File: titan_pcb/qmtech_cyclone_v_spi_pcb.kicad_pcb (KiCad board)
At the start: 2 copper layers, 101.6 x 88.9 mm, 13 parts, among them J1 FPGA U8, J15 teensy3.2_left_header_double, J16 pico_right_header_double, J2 FPGA U7, J3 DUMMY_JTAG, J4 esp_right_header_double, J5 pico_left_header_double, J7 esp_left_header_double, J8 teensy3.2_right_header_double, U1 ESP32-DevKitC, U2 Teensy3.2, U3 Pico

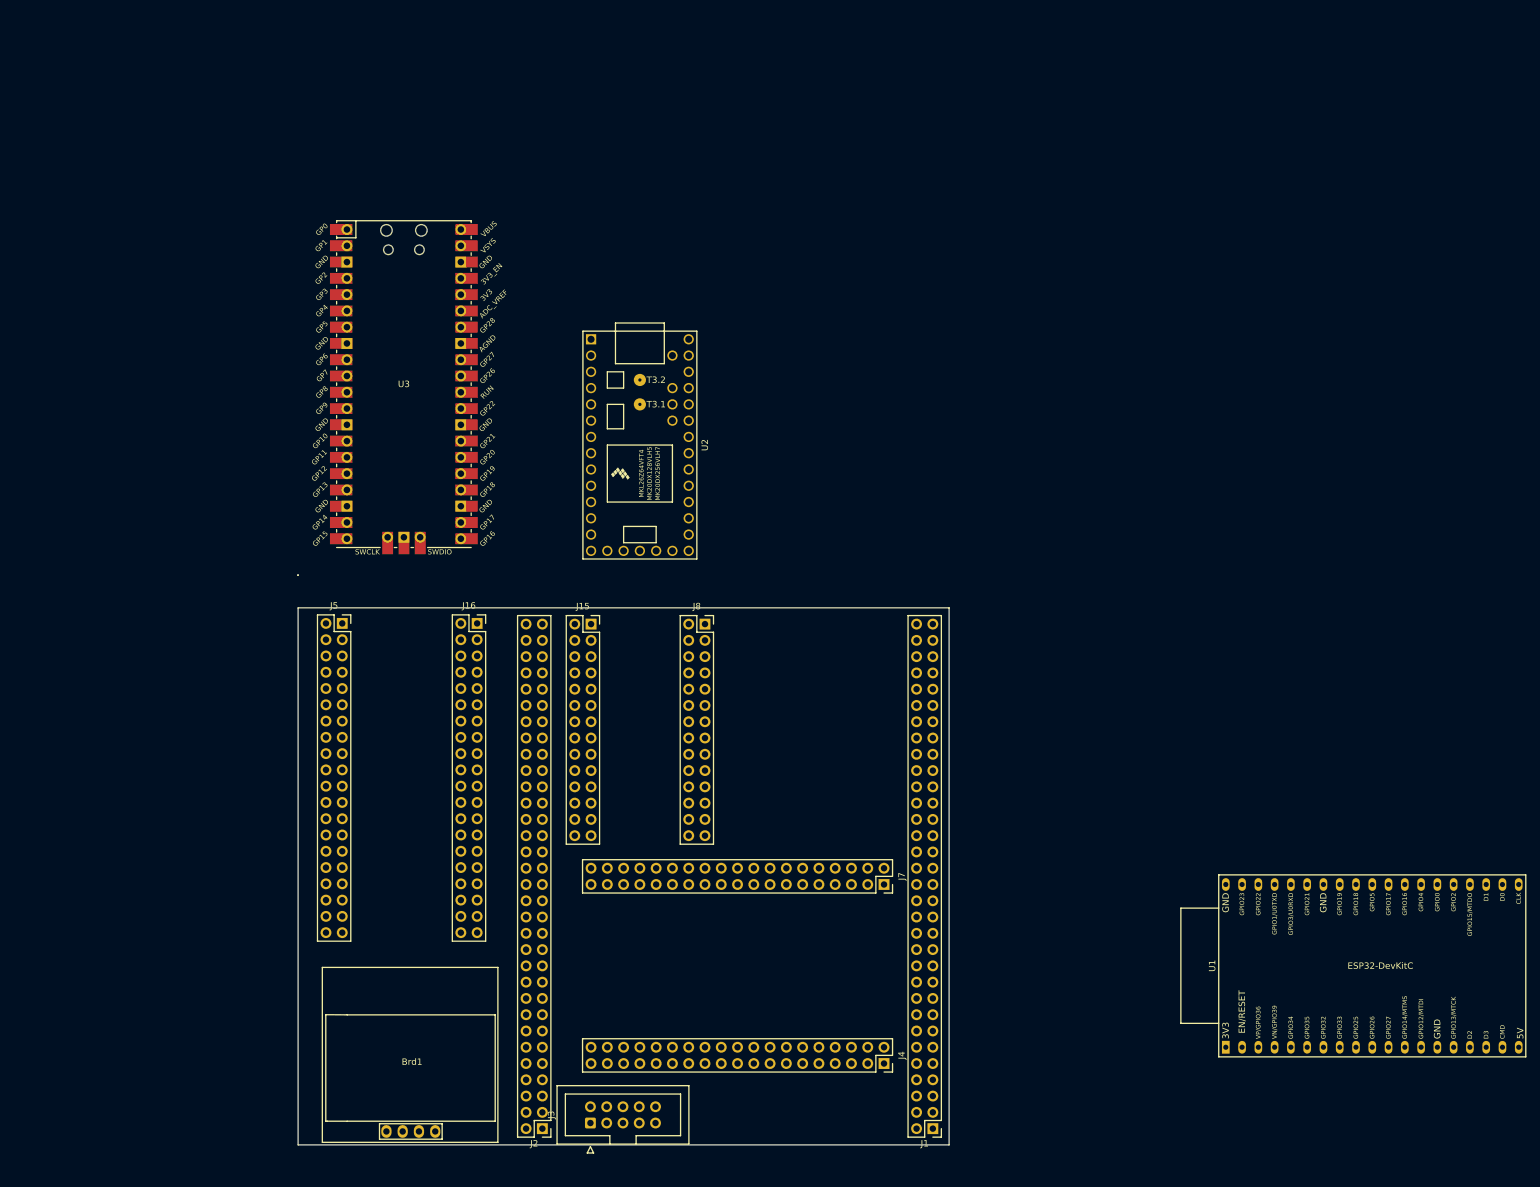
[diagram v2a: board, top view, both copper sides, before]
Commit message: finalised pcb - pinouts checked, silkscreen  and ground plane added
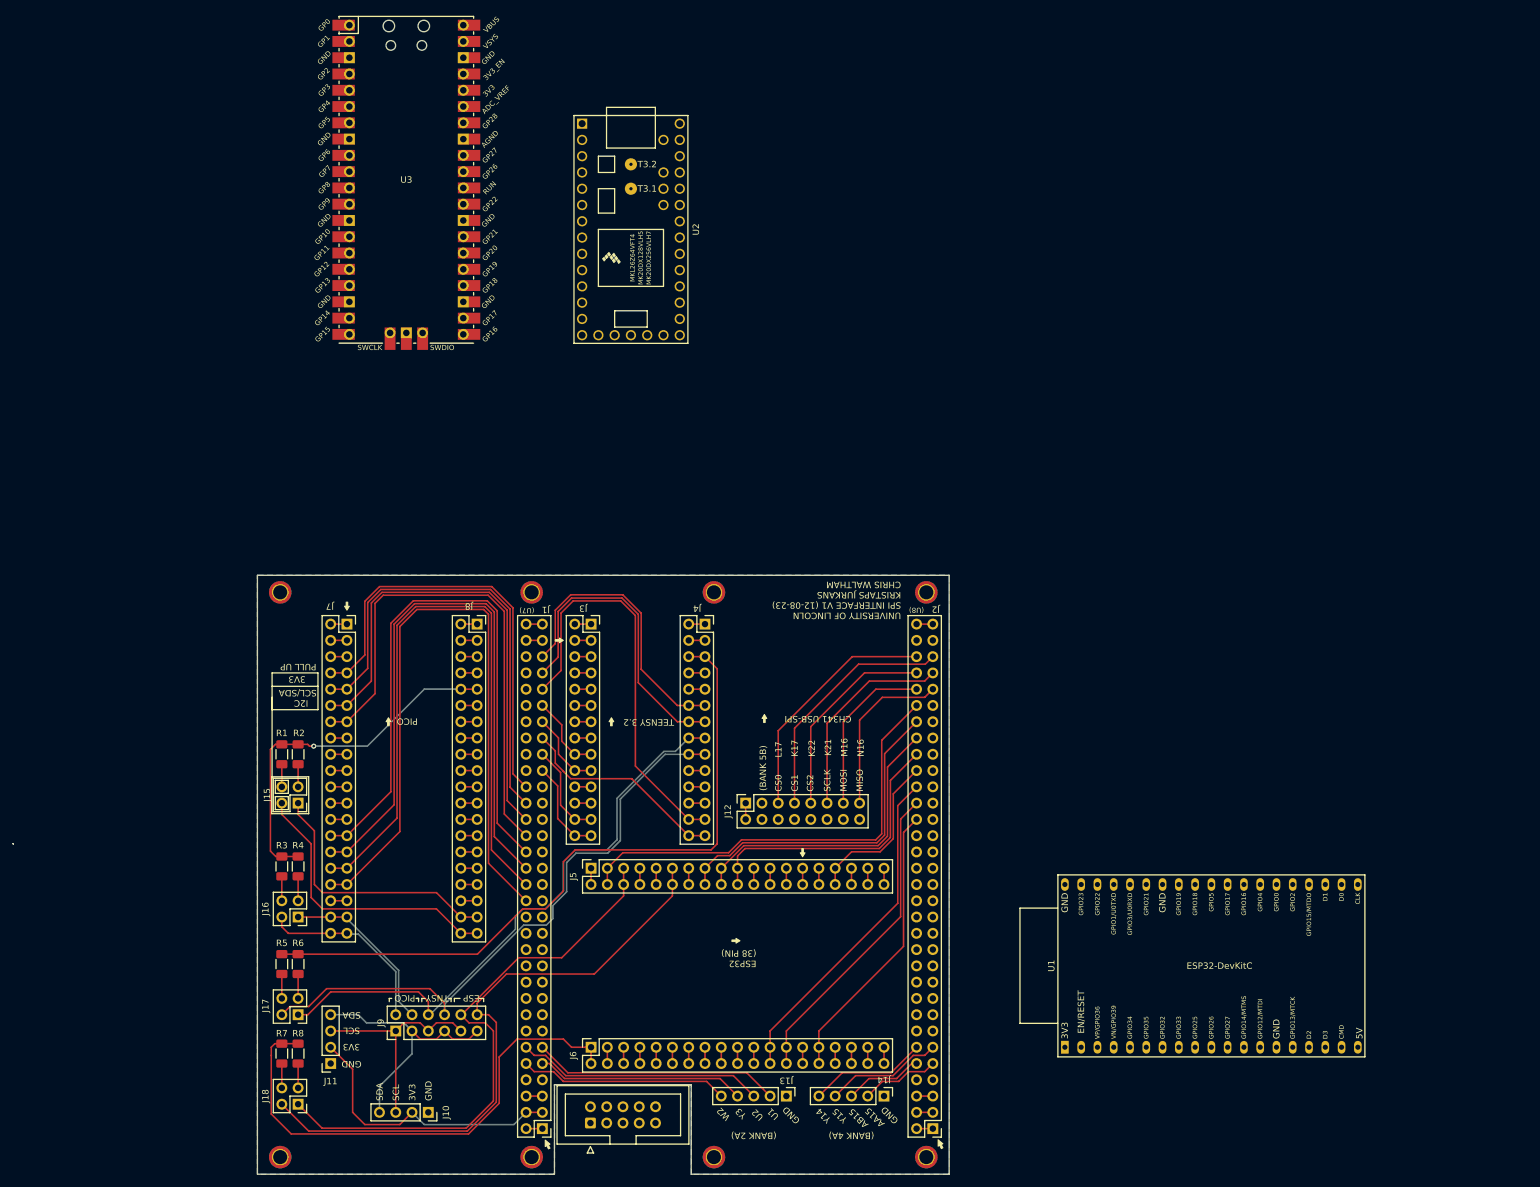
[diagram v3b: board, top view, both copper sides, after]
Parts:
- removed Brd1: OLED, SSD1306:128x64OLED
- added H1: MountingHole, MountingHole:MountingHole_2.2mm_M2_ISO7380_Pad_TopBottom, F.Cu at (48.0, 33.1)
- added H2: MountingHole, MountingHole:MountingHole_2.2mm_M2_ISO7380_Pad_TopBottom, F.Cu at (48.0, 121.3)
- added H3: MountingHole, MountingHole:MountingHole_2.2mm_M2_ISO7380_Pad_TopBottom, F.Cu at (87.2, 33.1)
- added H4: MountingHole, MountingHole:MountingHole_2.2mm_M2_ISO7380_Pad_TopBottom, F.Cu at (87.2, 121.3)
- added H5: MountingHole, MountingHole:MountingHole_2.2mm_M2_ISO7380_Pad_TopBottom, F.Cu at (148.8, 33.1)
- added H6: MountingHole, MountingHole:MountingHole_2.2mm_M2_ISO7380_Pad_TopBottom, F.Cu at (148.8, 121.3)
- added H7: MountingHole, MountingHole:MountingHole_2.2mm_M2_ISO7380_Pad_TopBottom, F.Cu at (115.7, 33.1)
- added H8: MountingHole, MountingHole:MountingHole_2.2mm_M2_ISO7380_Pad_TopBottom, F.Cu at (115.7, 121.3)
- added J10: OLED_CONN_0, Connector_PinSocket_2.54mm:PinSocket_1x04_P2.54mm_Vertical, F.Cu at (71.1, 114.3)
- added J11: OLED_CONN_1, Connector_PinSocket_2.54mm:PinSocket_1x04_P2.54mm_Vertical, F.Cu at (55.9, 106.7)
- added J12: CH341_PRG_CONN, Connector_PinSocket_2.54mm:PinSocket_2x08_P2.54mm_Vertical, F.Cu at (120.7, 66.0)
- added J13: SPI_HEADER_0, Connector_PinHeader_2.54mm:PinHeader_1x05_P2.54mm_Vertical, F.Cu at (127.0, 111.8)
- added J14: SPI_HEADER_1, Connector_PinHeader_2.54mm:PinHeader_1x05_P2.54mm_Vertical, F.Cu at (142.2, 111.8)
- added J15: PICO_I2C0_PULLUPS, Connector_PinHeader_2.54mm:PinHeader_2x02_P2.54mm_Vertical, F.Cu at (50.8, 66.0)
- added J16: PICO_I2C1_PULLUPS, Connector_PinHeader_2.54mm:PinHeader_2x02_P2.54mm_Vertical, F.Cu at (50.8, 83.8)
- added J17: TEENSY_I2C_PULLUPS, Connector_PinHeader_2.54mm:PinHeader_2x02_P2.54mm_Vertical, F.Cu at (50.8, 99.1)
- added J18: ESP32_I2C_PULLUPS, Connector_PinHeader_2.54mm:PinHeader_2x02_P2.54mm_Vertical, F.Cu at (50.8, 113.0)
- added J9: OLED_JMP, Connector_PinHeader_2.54mm:PinHeader_2x06_P2.54mm_Vertical, F.Cu at (66.0, 101.6)
- added R1: 2K, Resistor_SMD:R_1206_3216Metric_Pad1.30x1.75mm_HandSolder, F.Cu at (48.3, 58.4)
- added R2: 2K, Resistor_SMD:R_1206_3216Metric_Pad1.30x1.75mm_HandSolder, F.Cu at (50.8, 58.4)
- added R3: 2K, Resistor_SMD:R_1206_3216Metric_Pad1.30x1.75mm_HandSolder, F.Cu at (48.3, 75.9)
- added R4: 2K, Resistor_SMD:R_1206_3216Metric_Pad1.30x1.75mm_HandSolder, F.Cu at (50.8, 75.9)
- added R5: 2K, Resistor_SMD:R_1206_3216Metric_Pad1.30x1.75mm_HandSolder, F.Cu at (48.3, 91.2)
- added R6: 2K, Resistor_SMD:R_1206_3216Metric_Pad1.30x1.75mm_HandSolder, F.Cu at (50.8, 91.2)
- added R7: 2K, Resistor_SMD:R_1206_3216Metric_Pad1.30x1.75mm_HandSolder, F.Cu at (48.3, 105.1)
- added R8: 2K, Resistor_SMD:R_1206_3216Metric_Pad1.30x1.75mm_HandSolder, F.Cu at (50.8, 105.1)
- J3: renamed from J15; value teensy3.2_left_header_double -> T3.2_LEFT_HEADER
- J4: renamed from J8; value teensy3.2_right_header_double -> T3.2_RIGHT_HEADER
- J5: renamed from J4; value esp_right_header_double -> ESP_LEFT_HEADER
- J6: renamed from J7; value esp_left_header_double -> ESP_RIGHT_HEADER
- J7: renamed from J5; value pico_left_header_double -> PICO_LEFT_HEADER
- J8: renamed from J16; value pico_right_header_double -> PICO_RIGHT_HEADER
- moved J5 54.9 mm to (96.5, 76.2), turned to 90 degrees
- moved J6 52.3 mm to (96.5, 104.1), turned to 90 degrees
- moved U2 33.7 mm to (102.7, -23.5)
- moved U3 31.9 mm to (67.7, -31.2)
- moved U1 25.1 mm to (170.5, 104.1)
- moved J7 0.74 mm to (58.4, 38.1)
- moved J8 0.11 mm to (78.7, 38.1)
- renumbered J2 to J1, J1 to J2, J3 to Jx1
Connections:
- net TEENSY_GPIO_18 renamed TEENSY_GPIO_18_SDA
- net TEENSY_GPIO_19 renamed TEENSY_GPIO_19_SCL
- J3 pad 1: TEENSY_GND -> GND
- J3 pad 17: BANK_7A_B15 -> BANK_7A_B13
- J3 pad 18: BANK_7A_B15 -> BANK_7A_B13
- J3 pad 19: BANK_7A_C15 -> BANK_7A_D13
- J3 pad 2: TEENSY_GND -> GND
- J3 pad 20: BANK_7A_C15 -> BANK_7A_D13
- J3 pad 25: BANK_7A_E12 -> BANK_7A_B12
- J3 pad 26: BANK_7A_E12 -> BANK_7A_B12
- J3 pad 27: BANK_7A_D12 -> BANK_7A_C11
- J3 pad 28: BANK_7A_D12 -> BANK_7A_C11
- J4 pad 13: BANK_7A_D13 -> BANK_7A_B15
- J4 pad 14: BANK_7A_D13 -> BANK_7A_B15
- J4 pad 25: BANK_7A_B16 -> BANK_7A_A15
- J4 pad 26: BANK_7A_B16 -> BANK_7A_A15
- J4 pad 27: BANK_7A_C13 -> BANK_7A_E12
- J4 pad 28: BANK_7A_C13 -> BANK_7A_E12
- J5 pad 1: ESP_GND -> GND
- J5 pad 13: ESP_GND -> GND
- J5 pad 14: ESP_GND -> GND
- J5 pad 15: BANK_5B_M20 -> BANK_5B_L19
- J5 pad 16: BANK_5B_M20 -> BANK_5B_L19
- J5 pad 19: BANK_5B_M18 -> BANK_5B_M20
- J5 pad 2: ESP_GND -> GND
- J5 pad 20: BANK_5B_M18 -> BANK_5B_M20
- J5 pad 3: BANK_5B_M21 -> BANK_5B_L22
- J5 pad 31: BANK_5B_N20 -> BANK_5B_N21
- J5 pad 32: BANK_5B_N20 -> BANK_5B_N21
- J5 pad 4: BANK_5B_M21 -> BANK_5B_L22
- J6 pad 23: BANK_5B_N21 -> BANK_5A_P17
- J6 pad 24: BANK_5B_N21 -> BANK_5A_P17
- J6 pad 25: BANK_5A_P17 -> BANK_5A_T19
- J6 pad 26: BANK_5A_P17 -> BANK_5A_T19
- J6 pad 27: ESP_GND -> GND
- J6 pad 28: ESP_GND -> GND
- J6 pad 29: BANK_5A_P16 -> BANK_5A_R21
- J6 pad 30: BANK_5A_P16 -> BANK_5A_R21
- J7 pad 10: BANK_8A_B10 -> BANK_8A_C9
- J7 pad 11: BANK_8A_C9 -> BANK_8A_A10
- J7 pad 12: BANK_8A_C9 -> BANK_8A_A10
- J7 pad 13: BANK_8A_G10 -> BANK_8A_A8
- J7 pad 14: BANK_8A_G10 -> BANK_8A_A8
- J7 pad 15: PICO_GND -> GND
- J7 pad 16: PICO_GND -> GND
- J7 pad 17: BANK_8A_B7 -> PICO_SPI0_SCLK_I2C1_SDA_GPIO6
- J7 pad 18: BANK_8A_B7 -> PICO_SPI0_SCLK_I2C1_SDA_GPIO6
- J7 pad 19: BANK_8A_B5 -> PICO_SPI0_DOUT_I2C1_SCL_GPIO7
- J7 pad 20: BANK_8A_B5 -> PICO_SPI0_DOUT_I2C1_SCL_GPIO7
- J7 pad 21: BANK_8A_A5 -> PICO_SPI1_DIN_I2C0_SDA_GPIO8
- J7 pad 22: BANK_8A_A5 -> PICO_SPI1_DIN_I2C0_SDA_GPIO8
- J7 pad 23: BANK_8A_B6 -> PICO_SPI1_CS_I2C0_SCL_GPIO9
- J7 pad 24: BANK_8A_B6 -> PICO_SPI1_CS_I2C0_SCL_GPIO9
- J7 pad 25: PICO_GND -> GND
- J7 pad 26: PICO_GND -> GND
- J7 pad 27: PICO_SPI1_SCLK_I2C1_SDA_GPIO10 -> BANK_8A_B7
- J7 pad 28: PICO_SPI1_SCLK_I2C1_SDA_GPIO10 -> BANK_8A_B7
- J7 pad 29: PICO_SPI1_DOUT_I2C_SCL_GPIO11 -> BANK_8A_A5
- J7 pad 30: PICO_SPI1_DOUT_I2C_SCL_GPIO11 -> BANK_8A_A5
- J7 pad 31: PICO_SPI1_DIN_I2C0_SDA_GPIO12 -> BANK_8A_D9
- J7 pad 32: PICO_SPI1_DIN_I2C0_SDA_GPIO12 -> BANK_8A_D9
- J7 pad 33: PICO_SPI1_CS_I2C0_SCL_GPIO13 -> BANK_8A_C6
- J7 pad 34: PICO_SPI1_CS_I2C0_SCL_GPIO13 -> BANK_8A_C6
- J7 pad 35: PICO_GND -> GND
- J7 pad 36: PICO_GND -> GND
- J7 pad 5: PICO_GND -> GND
- J7 pad 6: PICO_GND -> GND
- J7 pad 9: BANK_8A_B10 -> BANK_8A_C9
- J8 pad 15: PICO_GND -> GND
- J8 pad 16: PICO_GND -> GND
- J8 pad 25: PICO_GND -> GND
- J8 pad 26: PICO_GND -> GND
- J8 pad 35: PICO_GND -> GND
- J8 pad 36: PICO_GND -> GND
- J8 pad 5: PICO_GND -> GND
- J8 pad 6: PICO_GND -> GND
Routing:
- net TEENSY_3V3: track 0.00 -> 110.3 mm
- net BANK_8A_C6: track 0.00 -> 108.6 mm
- net BANK_8A_D9: track 0.00 -> 104.7 mm
- net BANK_8A_A5: track 0.00 -> 100.7 mm
- net BANK_8A_B7: track 0.00 -> 96.7 mm
- net ESP_I2C_SDA_GPIO21: track 0.00 -> 96.5 mm
- net TEENSY_GPIO_18_SDA: track 0.00 -> 95.9 mm
- net TEENSY_GPIO_19_SCL: track 0.00 -> 93.2 mm
- net ESP_I2C_SCL_GPIO22: track 0.00 -> 88.2 mm
- net BANK_8A_A8: track 0.00 -> 81.0 mm
- net ESP_3V3: track 0.00 -> 79.5 mm
- net BANK_8A_A10: track 0.00 -> 77.0 mm
- net BANK_8A_C9: track 0.00 -> 73.1 mm
- net BANK_5B_L22: track 0.00 -> 69.9 mm
- net BANK_8A_F10: track 0.00 -> 69.1 mm
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- added copper zone on B.Cu, net GND
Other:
- board size 101.6 x 88.9 mm -> 146.1 x 93.5 mm
- board text added: "(BANK 2A)"
- board text added: "(BANK 4A)"
- board text added: "(BANK 5B)"
- board text added: "(U7)"
- board text added: "(U8)"
- board text added: "3V3"
- board text added: "AA15"
- board text added: "AB15"
- board text added: "CH341 USB-SPI"
- board text added: "CS0"
- board text added: "CS1"
- board text added: "CS2"
- board text added: "ESP"
- board text added: "ESP32 (38 PIN)"
- board text added: "GND"
- board text added: "I2C SCL/SDA"
- board text added: "K17"
- board text added: "K21"
- board text added: "K22"
- board text added: "L17"
- board text added: "M16"
- board text added: "MISO"
- board text added: "MOSI"
- board text added: "N16"
- board text added: "PICO"
- board text added: "PULL UP"
- board text added: "SCL"
- board text added: "SCLK"
- board text added: "SDA"
- board text added: "TEENSY 3.2"
- board text added: "TNSY"
- board text added: "U1"
- board text added: "U2"
- board text added: "UNIVERSITY OF LINCOLN SPI INTERFACE V1 (12-08-23) KRISTAPS JURKANS CHRIS WALTHAM"
- board text added: "W2"
- board text added: "Y14"
- board text added: "Y15"
- board text added: "Y3"

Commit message: made dimensions nicer, moved screw holes as to not interfer with FPGA
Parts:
- moved H6 1.52 mm to (148.9, 122.8)
- moved H2 1.52 mm to (48.0, 122.8)
- moved H4 1.52 mm to (87.2, 122.8)
- moved H8 1.52 mm to (115.7, 122.8)
- moved H5 0.05 mm to (148.9, 33.1)
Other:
- board size 146.1 x 93.5 mm -> 146.1 x 95 mm
- board text added: "krisj.dev github/arkis-s/titan"

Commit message: (wip) drawing 3v3 supply
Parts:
- removed U2: Teensy3.2, teensy:Teensy30_31_32_LC
- removed U3: Pico, MCU_RaspberryPi_and_Boards:RPi_Pico_SMD_TH
- added C1: 10uF, Capacitor_Tantalum_SMD:CP_EIA-3216-18_Kemet-A_Pad1.58x1.35mm_HandSolder, F.Cu at (140.9, 110.3)
- added C2: 10uF, Capacitor_Tantalum_SMD:CP_EIA-3216-18_Kemet-A_Pad1.58x1.35mm_HandSolder, F.Cu at (130.7, 122.4)
- added J19: Barrel_Jack_MountingPin, Connector_BarrelJack:BarrelJack_CUI_PJ-063AH_Horizontal, F.Cu at (139.4, 113.4)
- added J20: Conn_01x02, Connector_PinHeader_2.54mm:PinHeader_1x02_P2.54mm_Vertical, F.Cu at (48.3, 38.1)
- added J21: Conn_01x02, Connector_PinHeader_2.54mm:PinHeader_1x02_P2.54mm_Vertical, F.Cu at (117.6, 40.6)
- added J22: Conn_01x02, Connector_PinHeader_2.54mm:PinHeader_1x02_P2.54mm_Vertical, F.Cu at (93.5, 106.7)
- added Ux1: ESP32-DevKitC, PCM_Espressif:ESP32-DevKitC, F.Cu at (163.4, 119.5)
- added Ux2: Teensy3.2, teensy:Teensy30_31_32_LC, F.Cu at (233.3, 235.4)
- added Ux3: Pico, MCU_RaspberryPi_and_Boards:RPi_Pico_SMD_TH, F.Cu at (255.3, 271.4)
- U1: value ESP32-DevKitC -> LM1084-3.3; footprint PCM_Espressif:ESP32-DevKitC -> Package_TO_SOT_SMD:TO-263-3_TabPin2
- moved J14 64.3 mm to (78.7, 121.9)
- moved J13 64.3 mm to (63.5, 121.9)
- moved U1 50.5 mm to (121.0, 114.7), turned to 180 degrees
- moved J12 1.20 mm to (121.7, 66.7)
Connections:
- J1 pad 3: 3V3 -> FPGA_3V3
- J1 pad 4: 3V3 -> FPGA_3V3
- J13 pad 4: BANK_2A_Y3 -> BANK_2A_N1
- J13 pad 5: BANK_2A_W2 -> BANK_2A_N2
- J14 pad 2: BANK_4A_AA15 -> BANK_2A_AA2
- J14 pad 3: BANK_4A_AB15 -> BANK_2A_AA1
- J14 pad 4: BANK_4A_Y15 -> BANK_2A_Y3
- J14 pad 5: BANK_4A_Y14 -> BANK_2A_W2
- J2 pad 3: 3V3 -> FPGA_3V3
- J2 pad 4: 3V3 -> FPGA_3V3
- U1 pad 1: unconnected-(U1-3V3-Pad1) -> GND
- U1 pad 2: unconnected-(U1-CHIP_PU-Pad2) -> 3V3
- U1 pad 3: unconnected-(U1-SENSOR_VP/GPIO36/ADC1_CH0-Pad3) -> Net-(U1-VI)
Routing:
- net TEENSY_3V3: track 110.3 -> 8.38 mm
- net ESP_3V3: track 79.5 -> 8.13 mm
- net BANK_2A_N2: track 0.00 -> 44.1 mm
- net BANK_2A_N1: track 0.00 -> 44.1 mm
- net 3V3: track 46.9 -> 70.4 mm, vias 0 -> 6
- net BANK_2A_AA2: track 0.00 -> 19.0 mm
- net BANK_4A_Y15: track 18.4 -> 0.00 mm
- net BANK_4A_Y14: track 18.4 -> 0.00 mm
- net BANK_2A_AA1: track 0.00 -> 18.0 mm
- net Net-(U1-VI): track 0.00 -> 15.2 mm
- net GND: track 43.2 -> 56.1 mm, vias 0 -> 4
- net BANK_4A_AA15: track 12.3 -> 0.00 mm
- net BANK_4A_AB15: track 12.3 -> 0.00 mm
- net BANK_2A_Y3: track 32.6 -> 24.9 mm
- net BANK_2A_W2: track 32.6 -> 25.7 mm
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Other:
- board text added: "TODO: add regular + supporting hardware - move aux spi headers to section below oled screen"

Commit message: updated silkscreen, added diode for pico power supply, consolidated part value fields for BOM
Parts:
- added D1: 1N4148, Diode_THT:D_DO-35_SOD27_P7.62mm_Horizontal, F.Cu at (71.3, 42.0)
- added J23: PWR_SW, Connector_PinHeader_2.54mm:PinHeader_1x02_P2.54mm_Vertical, F.Cu at (82.5, 34.4)
- J1: value FPGA U7 -> FPGA
- J10: value OLED_CONN_0 -> OLED_CONN
- J11: value OLED_CONN_1 -> OLED_CONN
- J13: value SPI_HEADER_0 -> SPI_HEADER
- J14: value SPI_HEADER_1 -> SPI_HEADER
- J15: value PICO_I2C0_PULLUPS -> I2C_PULLUP
- J16: value PICO_I2C1_PULLUPS -> I2C_PULLUP
- J17: value TEENSY_I2C_PULLUPS -> I2C_PULLUP
- J18: value ESP32_I2C_PULLUPS -> I2C_PULLUP
- J2: value FPGA U8 -> FPGA
- J20, J21, J22: value Conn_01x02 -> PWR_SW
- J3: value T3.2_LEFT_HEADER -> TEENSY
- J4: value T3.2_RIGHT_HEADER -> TEENSY
- J5: value ESP_LEFT_HEADER -> ESP
- J6: value ESP_RIGHT_HEADER -> ESP
- J7: value PICO_LEFT_HEADER -> PICO
- J8: value PICO_RIGHT_HEADER -> PICO
- moved UX2 149.1 mm to (242.1, 86.6)
- moved UX3 149.1 mm to (264.1, 122.6)
- moved J20 30.7 mm to (78.7, 34.4), turned to -90 degrees
- moved UX1 15.6 mm to (167.9, 104.5)
- moved J21 5.09 mm to (117.3, 45.7), turned to 180 degrees
- renumbered Jx1 to JX1, Ux1 to UX1, Ux2 to UX2, Ux3 to UX3
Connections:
- net VIN renamed FPGA_VIN
- J15 pad 1: PICO_SPI0_CS_I2C0_SCL_GPIO17 -> PICO_SPI1_CS_I2C0_SCL_GPIO9
- J15 pad 2: PICO_SPI0_DIN_I2C0_SDA_GPIO16 -> PICO_SPI1_DIN_I2C0_SDA_GPIO8
- J20 pad 2: PICO_3V3 -> Net-(D1-A)
- R1 pad 2: PICO_3V3 -> 3V3
- R2 pad 2: PICO_3V3 -> 3V3
- R3 pad 2: PICO_3V3 -> 3V3
- R4 pad 2: PICO_3V3 -> 3V3
- R5 pad 2: TEENSY_3V3 -> 3V3
- R6 pad 2: TEENSY_3V3 -> 3V3
- R7 pad 2: ESP_3V3 -> 3V3
- R8 pad 2: ESP_3V3 -> 3V3
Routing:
- net 3V3: track 70.4 -> 369.6 mm, vias 6 -> 10
- net BANK_8A_C6: track 108.6 -> 50.9 mm
- net PICO_3V3: track 56.9 -> 2.54 mm, vias 1 -> 0
- net BANK_8A_D9: track 104.7 -> 55.8 mm
- net PICO_SPI0_DIN_I2C0_SDA_GPIO16: track 44.8 -> 2.54 mm
- net BANK_8A_A5: track 100.7 -> 58.4 mm
- net PICO_SPI0_CS_I2C0_SCL_GPIO17: track 41.3 -> 2.54 mm
- net GND: track 56.1 -> 91.0 mm, vias 4 -> 6
- net BANK_8A_B7: track 96.7 -> 63.6 mm
- net BANK_8A_F10: track 69.1 -> 94.5 mm
- net BANK_8A_C9: track 73.1 -> 89.3 mm
- net PICO_SPI1_DIN_I2C0_SDA_GPIO8: track 2.54 -> 11.2 mm
- net BANK_8A_A10: track 77.0 -> 85.4 mm
- net PICO_VSYS: track 2.54 -> 7.97 mm
- net PICO_SPI1_CS_I2C0_SCL_GPIO9: track 2.54 -> 7.62 mm
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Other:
- board text added: "AA1"
- board text added: "AA2"
- board text added: "BANK 2A"
- board text added: "IN: 2.6-29V"
- board text added: "N1"
- board text added: "N2"
- board text added: "OLED"
- board text added: "OUT: 3.3V, 5A MAX."
- board text added: "TODO: - ESP power supply?"
- board text removed: "(BANK 2A)"
- board text removed: "(BANK 4A)"
- board text removed: "AA15"
- board text removed: "AB15"
- board text removed: "TODO: add regular + supporting hardware - move aux spi headers to section below oled screen"
- board text removed: "Y14"
- board text removed: "Y15"
